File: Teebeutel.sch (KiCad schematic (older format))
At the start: 133 parts, among them J1 RJ45_Shielded, J2 Micro_SD_Card, J3 Battery, J4 Conn_01x30_Female, Q1 S8050, Q2 S8050, SW1 K1-1506SN-01, SW2 SW_SPST, U1 LIS2DE12, U10 SDB628, U11 TLV1117-33, U2 ESP32-WROOM-32, U3 RM-V8xxC_TR1, U4 TXB0104RUT, U5 TXB0104RUT, U6 SGP30, U7 PPSI262, U8 MCP73831-2-OT, U9 TLV70018_SOT23-5

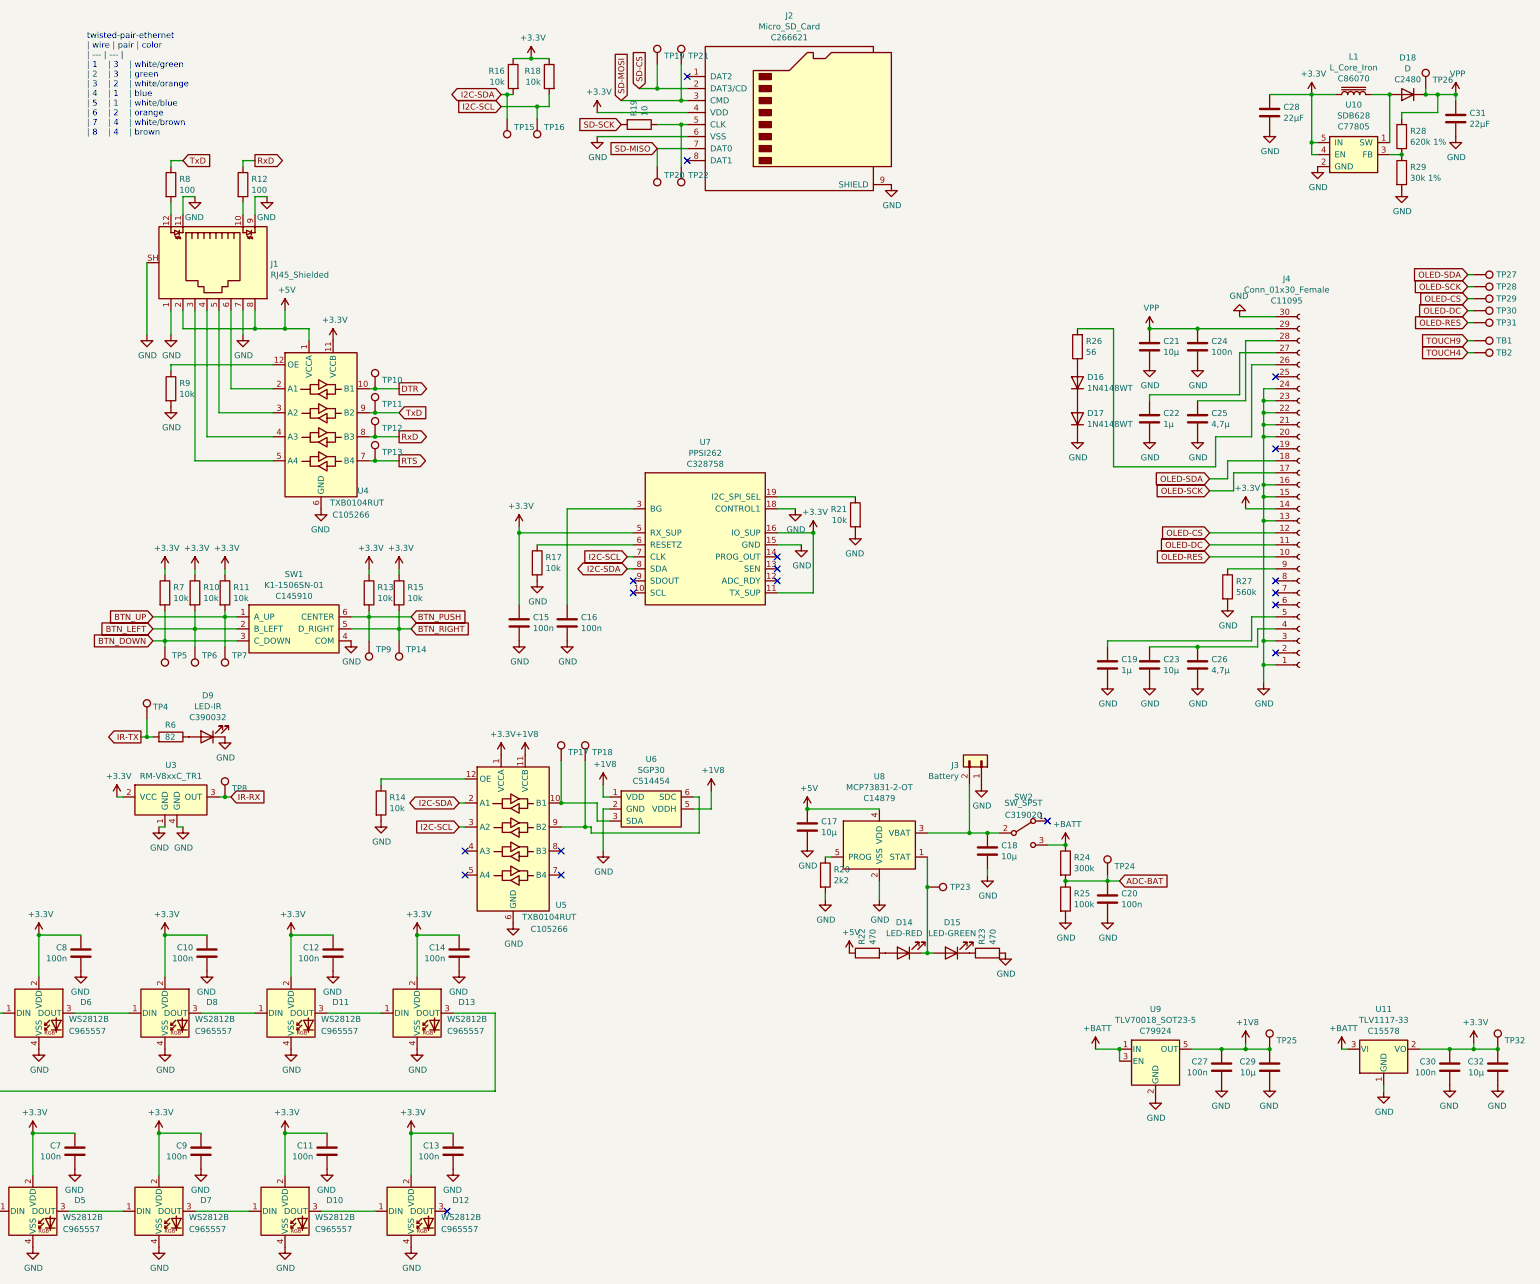
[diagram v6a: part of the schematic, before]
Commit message: fix+cleanup: more cleanup and fixes, retouched all Cs
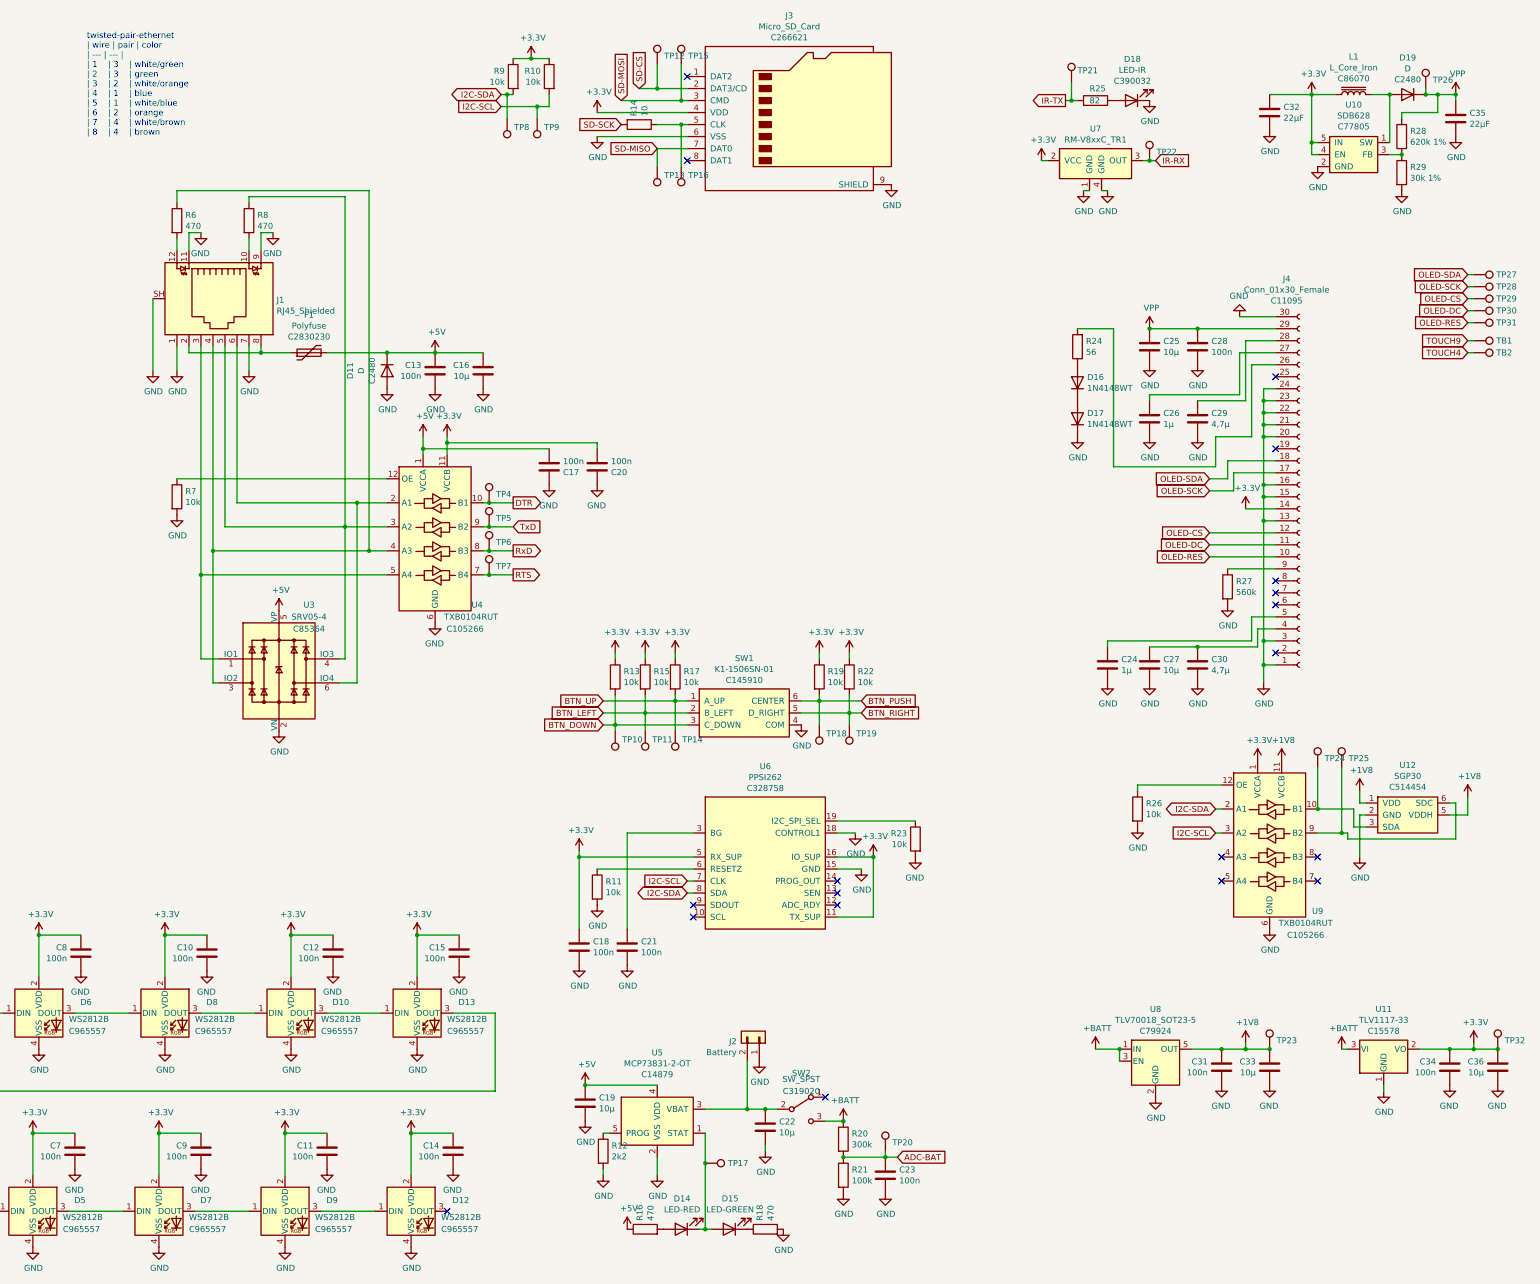
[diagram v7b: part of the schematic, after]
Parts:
- removed R12: 100, Resistor_SMD:R_0603_1608Metric, symbol Device:R
- added C13, C17, C20: 100n, Capacitor_SMD:C_0603_1608Metric, symbol Device:C
- added C16: 10µ, Capacitor_SMD:C_0603_1608Metric, symbol Device:C
- added D11: D, Diode_SMD:D_SMA, symbol Device:D
- added F1: Polyfuse, Fuse:Fuse_0805_2012Metric, symbol Device:Polyfuse
- added R6: 470, Resistor_SMD:R_0603_1608Metric, symbol Device:R
- added U3: SRV05-4, Package_TO_SOT_SMD:SOT-23-6, symbol Power_Protection:SRV05-4
- R8: value 100 -> 470; JLC 0603 -> R0603; LCSC C22775 -> C116694
- renumbered C13 to C14, C14 to C15, C15 to C18, C17 to C19, C16 to C21, C18 to C22, C20 to C23, C19 to C24, C21 to C25, C22 to C26, C23 to C27, C24 to C28, C25 to C29, C26 to C30, C27 to C31, C28 to C32, C29 to C33, C30 to C34, C31 to C35, C32 to C36, D11 to D10, D9 to D18, D18 to D19, D10 to D9, J3 to J2, J2 to J3, R18 to R10, R17 to R11, R20 to R12, R7 to R13, R19 to R14, R10 to R15, R22 to R16, R11 to R17, R23 to R18, R13 to R19, R24 to R20, R25 to R21, R15 to R22, R21 to R23, R26 to R24, R6 to R25, R14 to R26, R9 to R7, R16 to R9, TP5 to TP10, TP6 to TP11, TP19 to TP12, TP20 to TP13, TP7 to TP14, TP21 to TP15, TP22 to TP16, TP23 to TP17, TP9 to TP18, TP14 to TP19, TP24 to TP20, TP4 to TP21, TP8 to TP22, TP25 to TP23, TP17 to TP24, TP18 to TP25, TP10 to TP4, TP11 to TP5, TP12 to TP6, TP13 to TP7, TP15 to TP8, TP16 to TP9, U6 to U12, U8 to U5, U7 to U6, U3 to U7, U9 to U8, U5 to U9
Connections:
- net +3V3: now also C20.2
- net +5V: now also C13.1, C16.1, C17.2, D11.1 (K), F1.2, U3.5 (VP); no longer J1.2, J1.8
- net GND: now also C13.2, C16.2, C17.1, C20.1, D11.2 (A), U3.2 (VN)
- net TxD: no longer R8.1
- net at J1.10: now also R8.2
- net at J1.12: now also R6.2; no longer R8.2
- net at J1.3, U4.5 (A4): now also U3.1 (IO1)
- net at J1.4, U4.4 (A3): now also R6.1, U3.3 (IO2)
- net at J1.5, U4.3 (A2): now also R8.1, U3.4 (IO3)
- net at J1.6, U4.2 (A1): now also U3.6 (IO4)
- new net: F1.1, J1.2, J1.8
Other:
- moved on the sheet: C18, C19, C21, C22, C23, D14, D15, D18, J1, J2, R11, R12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

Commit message: fix(D16, D17): Change part number
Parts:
- D16, D17: LCSC C393518 -> C727112
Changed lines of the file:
@@
 F 3 "https://www.diodes.com/assets/Datasheets/ds30396.pdf" H 12250 3600 50  0001 C CNN
 F 4 "SOD-523" H 12250 3600 50  0001 C CNN "JLC"
-F 5 "C393518" H 12250 3600 50  0001 C CNN "LCSC"
+F 5 "C727112" H 12250 3600 50  0001 C CNN "LCSC"
 	1    12250 3600
 	0    -1   -1   0
@@
 F 3 "https://www.diodes.com/assets/Datasheets/ds30396.pdf" H 12250 3900 50  0001 C CNN
 F 4 "SOD-523" H 12250 3900 50  0001 C CNN "JLC"
-F 5 "C393518" H 12250 3900 50  0001 C CNN "LCSC"
+F 5 "C727112" H 12250 3900 50  0001 C CNN "LCSC"
 	1    12250 3900
 	0    -1   -1   0
